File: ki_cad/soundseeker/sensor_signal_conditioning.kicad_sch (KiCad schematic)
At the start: 0 parts

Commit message: schematic
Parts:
- added C?: 10n, Capacitor_SMD:C_0805_2012Metric_Pad1.18x1.45mm_HandSolder, symbol Device:C
- added C?: 10u, Resistor_SMD:R_1206_3216Metric_Pad1.30x1.75mm_HandSolder, symbol Device:C
- added C?: 101 cap code, Capacitor_SMD:C_0805_2012Metric_Pad1.18x1.45mm_HandSolder, symbol Device:C
- added C?: 100n, Capacitor_SMD:C_0805_2012Metric_Pad1.18x1.45mm_HandSolder, symbol Device:C
- added C? (x4): 1u, Resistor_SMD:R_0805_2012Metric_Pad1.20x1.40mm_HandSolder, symbol Device:C
- added R? (x2): 20k, Resistor_SMD:R_0805_2012Metric_Pad1.20x1.40mm_HandSolder, symbol Device:R
- added R?: 2.2k, Resistor_SMD:R_0805_2012Metric_Pad1.20x1.40mm_HandSolder, symbol Device:R
- added R?: 220, Resistor_SMD:R_0805_2012Metric_Pad1.20x1.40mm_HandSolder, symbol Device:R
- added U?: MAX11115, Package_TO_SOT_SMD:SOT-23-6_Handsoldering, symbol soundseeker:MAX11115
- added U?: MCP6476T-E/OT, Package_TO_SOT_SMD:SOT-23-5, symbol piezo_preamp:MCP6476T-E/OT
- added U?: NCP163, Package_TO_SOT_SMD:SOT-23-5_HandSoldering, symbol soundseeker:NCP163
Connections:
- new net: C?.2, R?.1
- new net: C?.2, R?.2, U?.1, U?.3 (AIN)
- new net: C?.1, R?.1, R?.2, U?.3 (+)
- new net: C?.1, R?.1, R?.2, U?.4 (-)
- new net +5V: C?.1, U?.1 (IN)
- new net ADC_CS: U?.6 (CS)
- new net ADC_DOUT: U?.5 (DOUT)
- new net ADC_SLCK: U?.4 (SCLK)
- new net GND: C?.1, C?.2, C?.2, C?.2, C?.2, C?.2, R?.2, U?.2 (GND), U?.2 (GND), U?.2 (V-)
- new net enable_analog_power_supply: U?.3 (EN)
- new net preamp_in: C?.1
- new net vcc_analog: C?.1, C?.1, C?.1, C?.2, R?.1, U?.1 (VDD), U?.5 (OUT), U?.5 (V+)
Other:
- note added: "recalc edges!"

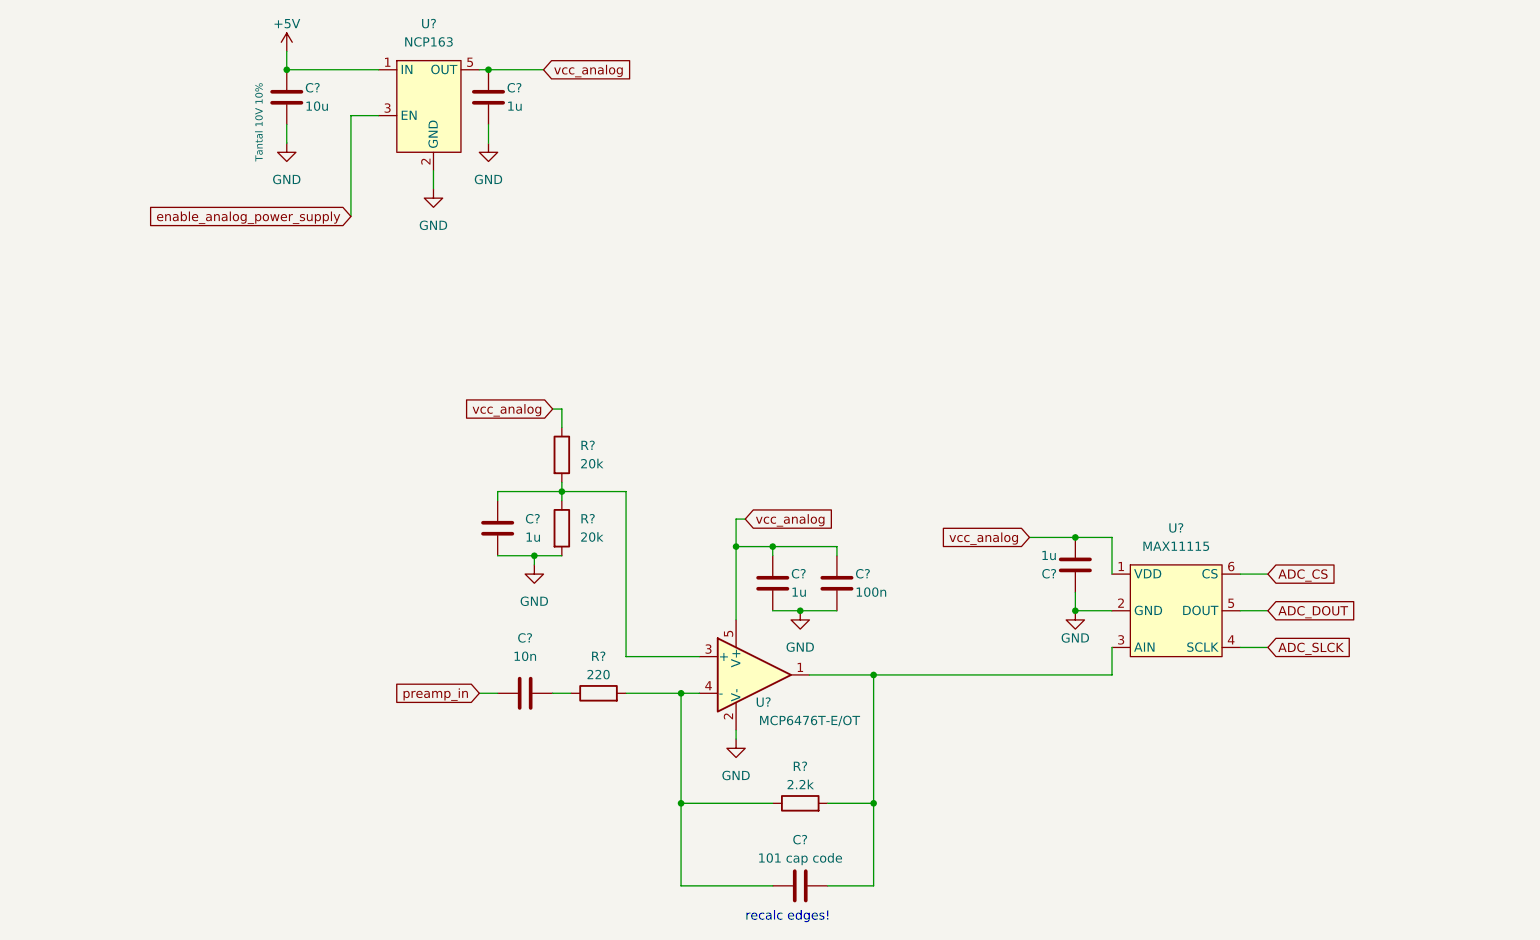
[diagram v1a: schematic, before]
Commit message: add buttons and display spi connections
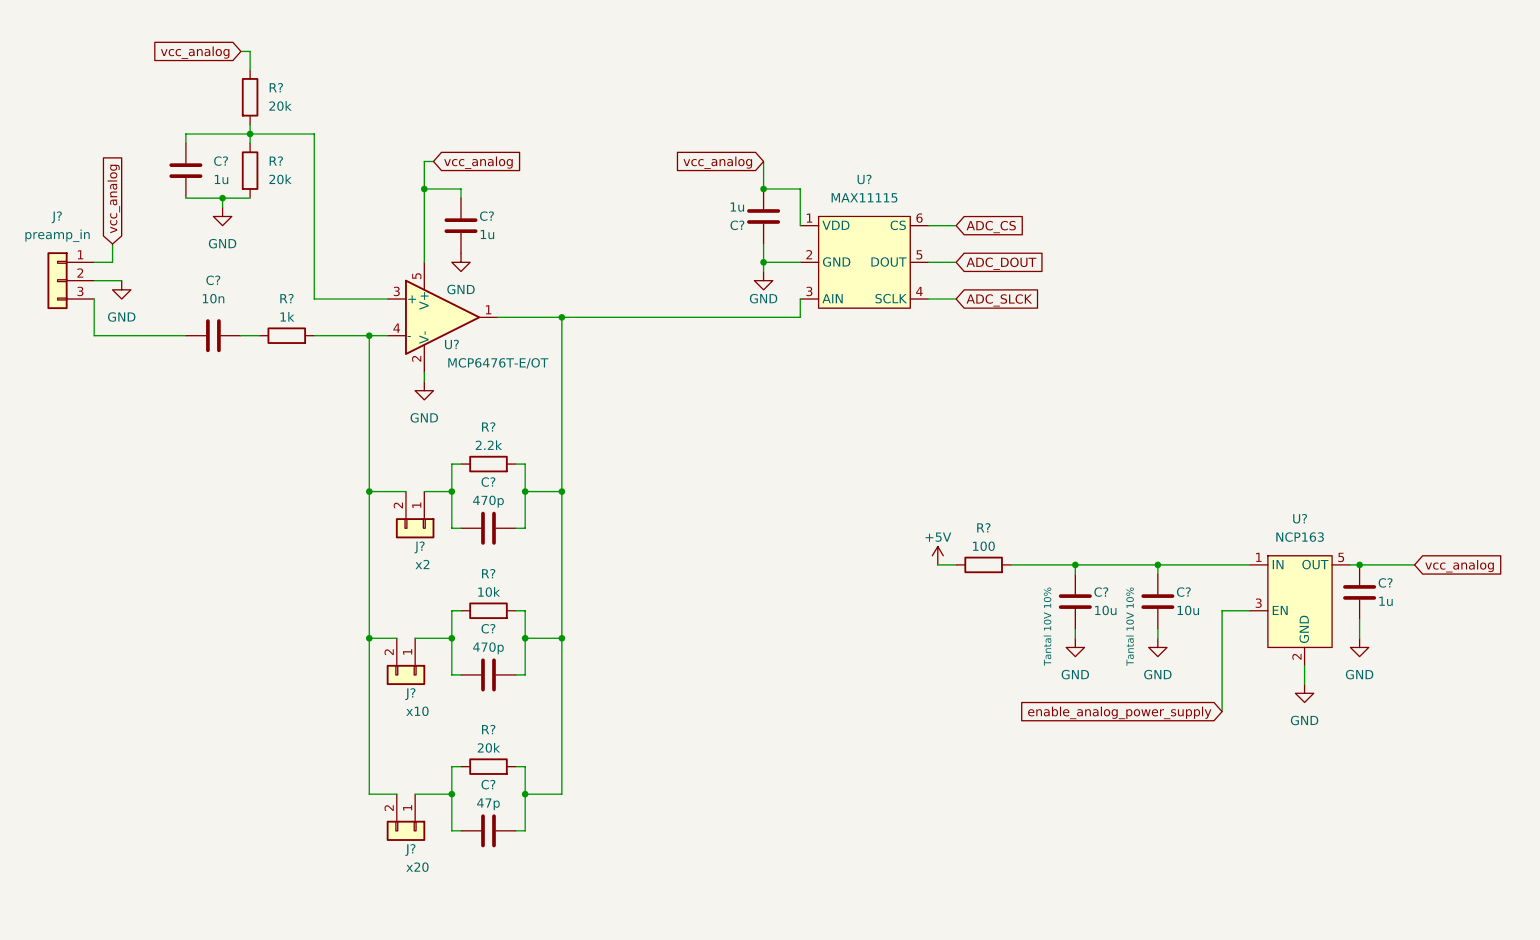
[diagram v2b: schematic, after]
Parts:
- removed C?: 100n, Capacitor_SMD:C_0805_2012Metric_Pad1.18x1.45mm_HandSolder, symbol Device:C
- added C?: 47p, Capacitor_SMD:C_0805_2012Metric_Pad1.18x1.45mm_HandSolder, symbol Device:C
- added C?: 10u, Resistor_SMD:R_1206_3216Metric_Pad1.30x1.75mm_HandSolder, symbol Device:C
- added C?: 470p, Capacitor_SMD:C_0805_2012Metric_Pad1.18x1.45mm_HandSolder, symbol Device:C
- added J?: x20, symbol Connector_Generic:Conn_01x02
- added J?: preamp_in, symbol Connector_Generic:Conn_01x03
- added J?: x10, symbol Connector_Generic:Conn_01x02
- added J?: x2, symbol Connector_Generic:Conn_01x02
- added R?: 100, Resistor_SMD:R_0805_2012Metric_Pad1.20x1.40mm_HandSolder, symbol Device:R
- added R?: 20k, Resistor_SMD:R_0805_2012Metric_Pad1.20x1.40mm_HandSolder, symbol Device:R
- added R?: 10k, Resistor_SMD:R_0805_2012Metric_Pad1.20x1.40mm_HandSolder, symbol Device:R
- C?: value 101 cap code -> 470p
- R?: value 220 -> 1k
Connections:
- net +5V: now also R?.1; no longer C?.1, U?.1 (IN)
- net GND: now also C?.2, J?.2 (Pin_2)
- net vcc_analog: now also J?.1 (Pin_1)
- net at C?.2, R?.2, U?.1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: now also C?.2, C?.2, R?.2, R?.2
- net at R?.2, U?.4 (-): now also J?.2 (Pin_2), J?.2 (Pin_2), J?.2 (Pin_2); no longer C?.1, R?.1
- net preamp_in: no longer names the net of C?.1
- net preamp_in: now also J?.3 (Pin_3)
- new net: C?.1, C?.1, R?.2, U?.1 (IN)
- new net: C?.1, J?.1 (Pin_1), R?.1 (x3)
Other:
- note removed: "recalc edges!"
- moved on the sheet: C?, R?, U?
